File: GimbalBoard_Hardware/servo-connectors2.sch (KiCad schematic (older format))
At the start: 44 parts, among them Q1 Q_NMOS_GDS, Q2 Q_NMOS_GDS, Q3 Q_NMOS_GDS, Q4 Q_NMOS_GDS, Q5 Q_NMOS_GDS, Q6 Q_NMOS_GDS, Q7 Q_NMOS_GDS, Q8 Q_NMOS_GDS

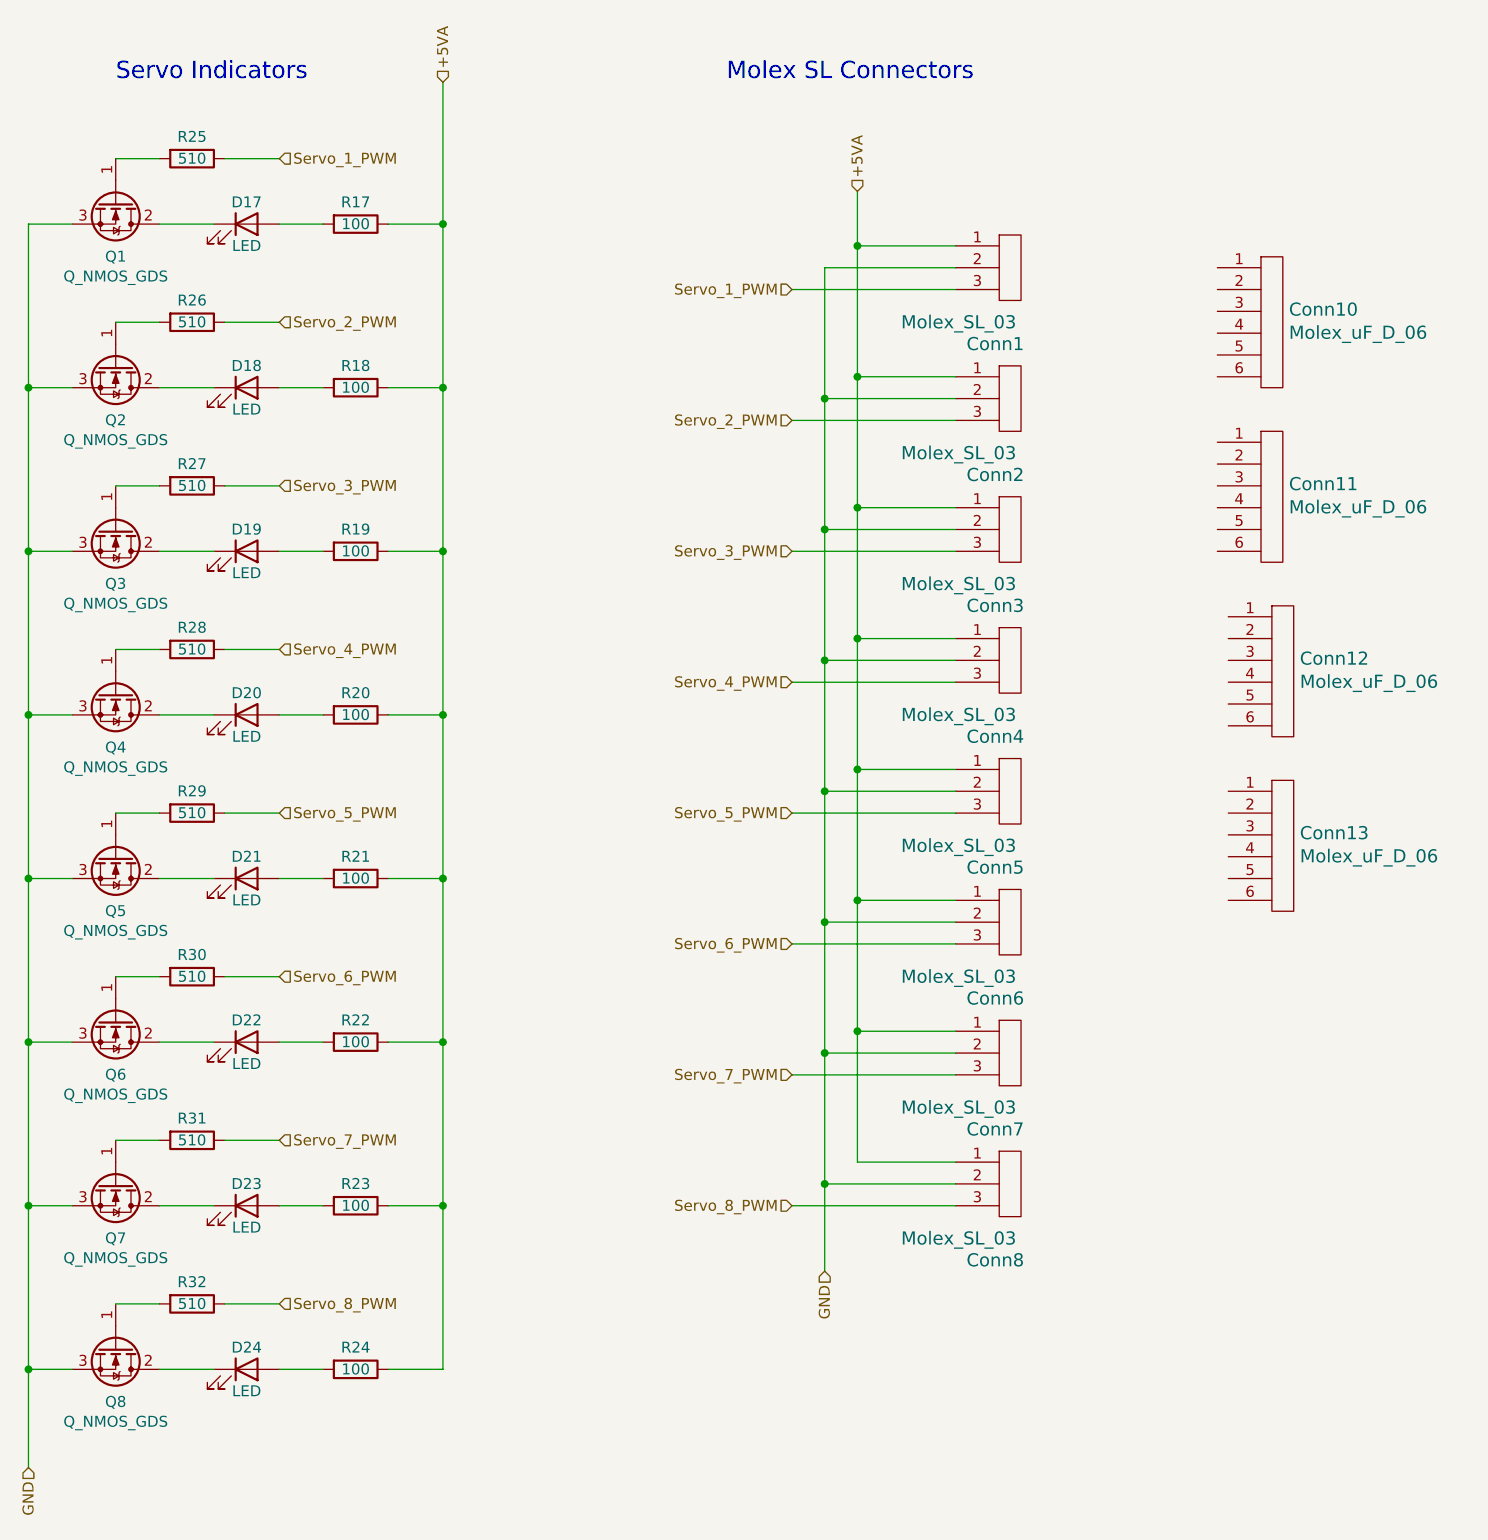
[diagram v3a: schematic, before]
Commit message: new connectors and decals
i have the 3x2 molex on here as well as some cowboy bebop decals.
the swtich still needs be confirmed.
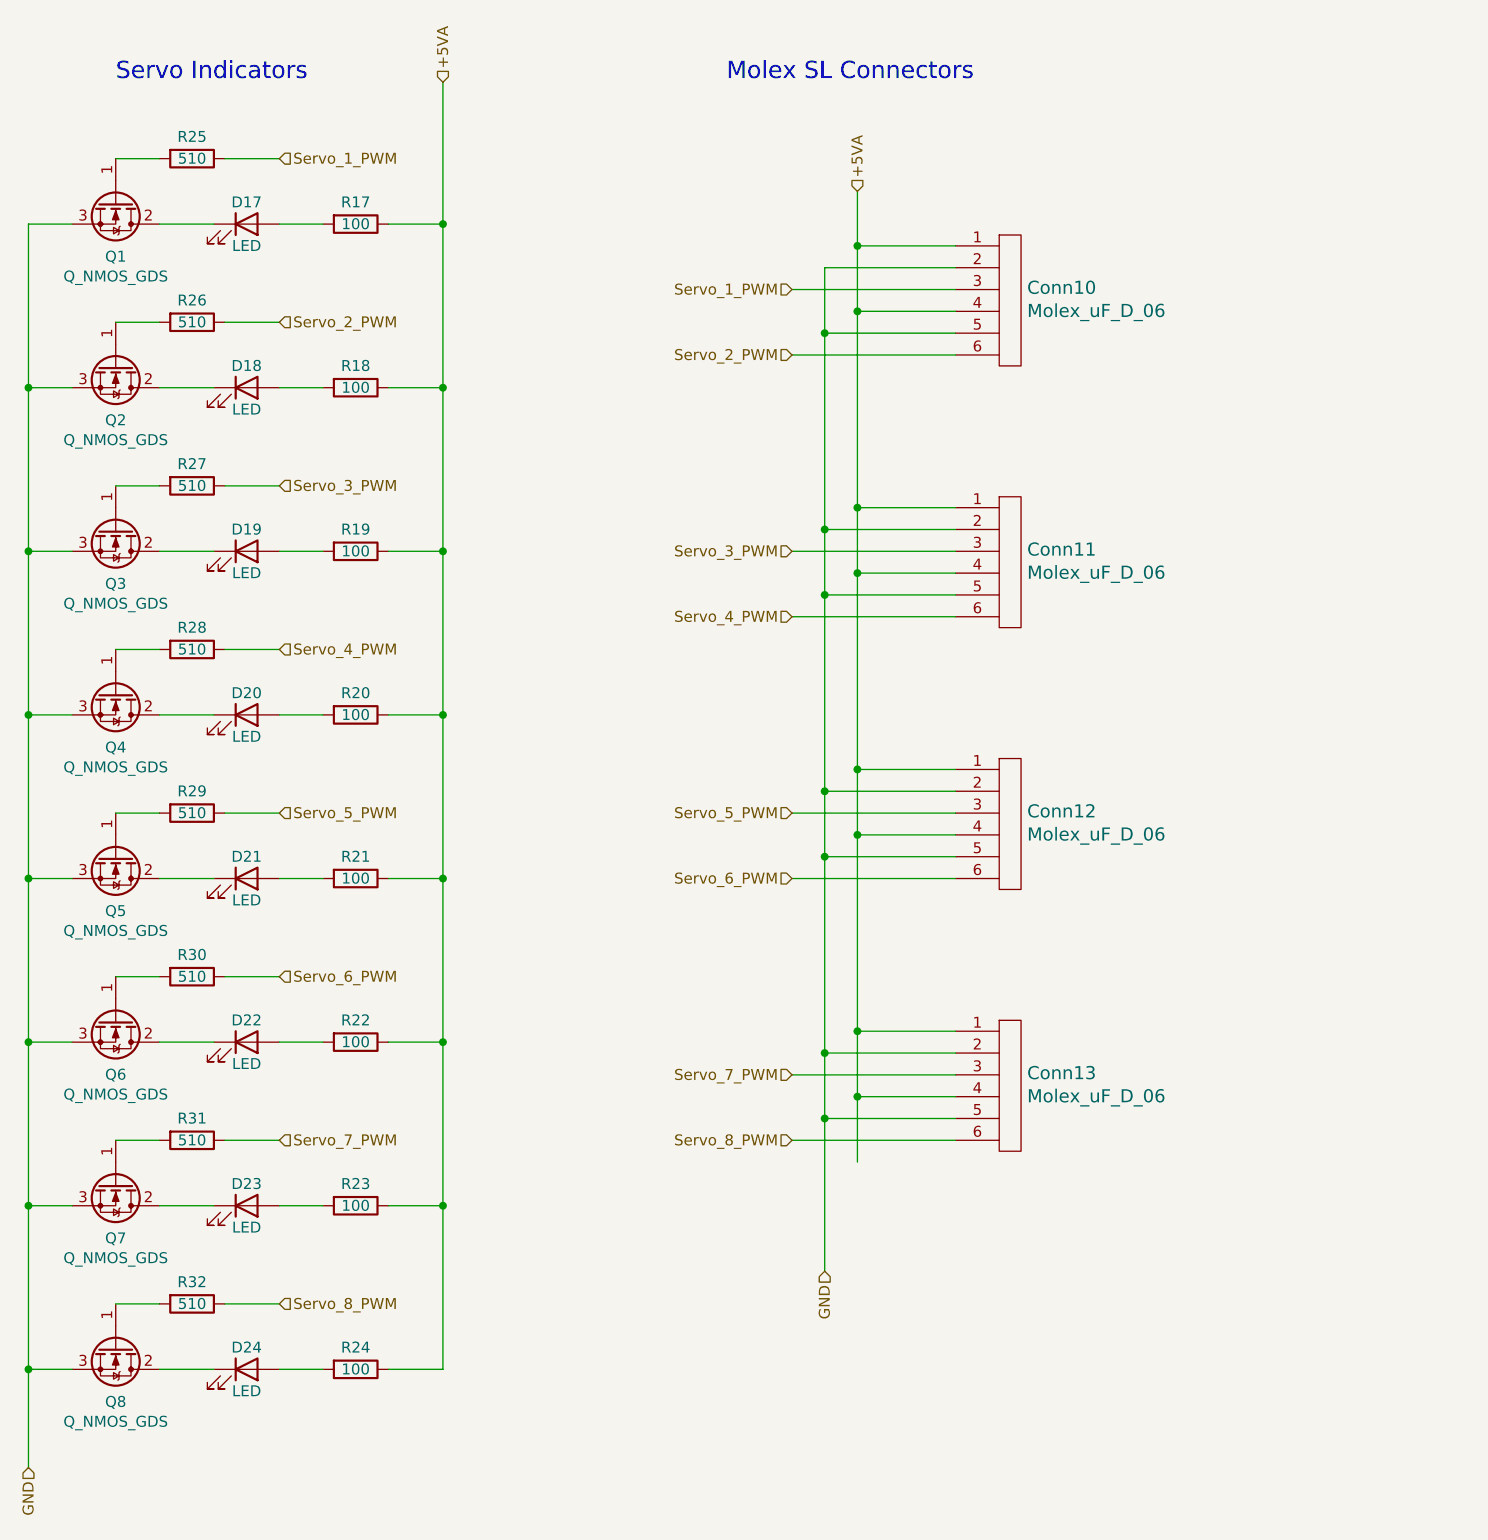
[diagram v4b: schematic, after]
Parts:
- removed Conn1, Conn2, Conn3, Conn4, Conn5, Conn6, Conn7, Conn8: Molex_SL_03, MRDT_Connectors:MOLEX_SL_03_Horizontal, symbol MRDT_Connectors:Molex_SL_03
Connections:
- net +5VA: now also Conn10.1, Conn10.4, Conn11.1, Conn11.4, Conn12.1, Conn12.4, Conn13.1, Conn13.4
- net GND: now also Conn10.2, Conn10.5, Conn11.2, Conn11.5, Conn12.2, Conn12.5, Conn13.2, Conn13.5
- net Servo_1_PWM: now also Conn10.3
- net Servo_2_PWM: now also Conn10.6
- net Servo_3_PWM: now also Conn11.3
- net Servo_4_PWM: now also Conn11.6
- net Servo_5_PWM: now also Conn12.3
- net Servo_6_PWM: now also Conn12.6
- net Servo_7_PWM: now also Conn13.3
- net Servo_8_PWM: now also Conn13.6
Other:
- moved on the sheet: Conn10, Conn11, Conn12, Conn13
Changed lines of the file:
@@
 Text HLabel 5000 6450 3    50   Input ~ 0
 GND
-Text HLabel 4850 6150 0    50   Input ~ 0
+Text HLabel 4850 5850 0    50   Input ~ 0
 Servo_8_PWM
-Connection ~ 5000 6050
 Wire Wire Line
-	5000 6050 5000 6450
+	5600 5850 4850 5850
 Wire Wire Line
-	5600 6150 4850 6150
+	5600 5750 5000 5750
 Wire Wire Line
-	5600 6050 5000 6050
-Wire Wire Line
-	5600 5950 5150 5950
-$Comp
-L MRDT_Connectors:Molex_SL_03 Conn?
-U 1 1 617A1B6D
-P 5800 6200
-AR Path="/615E206C/617A1B6D" Ref="Conn?"  Part="1"
-AR Path="/6178B814/617A1B6D" Ref="Conn8"  Part="1"
-F 0 "Conn8" H 5650 6000 60  0000 L CNN
-F 1 "Molex_SL_03" H 5350 6100 60  0000 L CNN
-F 2 "MRDT_Connectors:MOLEX_SL_03_Horizontal" H 5800 6200 60  0001 C CNN
-F 3 "" H 5800 6200 60  0001 C CNN
-	1    5800 6200
-	1    0    0    -1
-$EndComp
-$Comp
-L MRDT_Connectors:Molex_SL_03 Conn?
-U 1 1 617A1B73
-P 5800 5600
-AR Path="/615E206C/617A1B73" Ref="Conn?"  Part="1"
-AR Path="/6178B814/617A1B73" Ref="Conn7"  Part="1"
-F 0 "Conn7" H 5650 5400 60  0000 L CNN
-F 1 "Molex_SL_03" H 5350 5500 60  0000 L CNN
-F 2 "MRDT_Connectors:MOLEX_SL_03_Horizontal" H 5800 5600 60  0001 C CNN
-F 3 "" H 5800 5600 60  0001 C CNN
-	1    5800 5600
-	1    0    0    -1
-$EndComp
+	5600 5650 5150 5650
 Text HLabel 4850 5550 0    50   Input ~ 0
 Servo_7_PWM
 Connection ~ 5000 5450
 Wire Wire Line
-	5000 6050 5000 5450
-Wire Wire Line
-	5150 5350 5150 5950
+	5150 5350 5150 5650
 Connection ~ 5150 5350
 Wire Wire Line
@@
 Wire Wire Line
 	5600 5350 5150 5350
-Text HLabel 4850 4950 0    50   Input ~ 0
+Text HLabel 4850 4650 0    50   Input ~ 0
 Servo_6_PWM
-Connection ~ 5000 4850
 Wire Wire Line
-	5000 5450 5000 4850
+	5600 4650 4850 4650
 Wire Wire Line
-	5150 4750 5150 5350
-Connection ~ 5150 4750
+	5600 4550 5000 4550
 Wire Wire Line
-	5600 4950 4850 4950
-Wire Wire Line
-	5600 4850 5000 4850
-Wire Wire Line
-	5600 4750 5150 4750
-$Comp
-L MRDT_Connectors:Molex_SL_03 Conn?
-U 1 1 617A1B79
-P 5800 5000
-AR Path="/615E206C/617A1B79" Ref="Conn?"  Part="1"
-AR Path="/6178B814/617A1B79" Ref="Conn6"  Part="1"
-F 0 "Conn6" H 5650 4800 60  0000 L CNN
-F 1 "Molex_SL_03" H 5350 4900 60  0000 L CNN
-F 2 "MRDT_Connectors:MOLEX_SL_03_Horizontal" H 5800 5000 60  0001 C CNN
-F 3 "" H 5800 5000 60  0001 C CNN
-	1    5800 5000
-	1    0    0    -1
-$EndComp
+	5600 4450 5150 4450
 Text HLabel 4850 4350 0    50   Input ~ 0
 Servo_5_PWM
-Connection ~ 5000 4250
 Wire Wire Line
-	5000 4850 5000 4250
-Wire Wire Line
-	5150 4150 5150 4750
-Connection ~ 5150 4150
+	5150 4150 5150 4450
 Wire Wire Line
 	5600 4350 4850 4350
@@
 Wire Wire Line
 	5600 4150 5150 4150
-$Comp
-L MRDT_Connectors:Molex_SL_03 Conn?
-U 1 1 617A1B7F
-P 5800 4400
-AR Path="/615E206C/617A1B7F" Ref="Conn?"  Part="1"
-AR Path="/6178B814/617A1B7F" Ref="Conn5"  Part="1"
-F 0 "Conn5" H 5650 4200 60  0000 L CNN
-F 1 "Molex_SL_03" H 5350 4300 60  0000 L CNN
-F 2 "MRDT_Connectors:MOLEX_SL_03_Horizontal" H 5800 4400 60  0001 C CNN
-F 3 "" H 5800 4400 60  0001 C CNN
-	1    5800 4400
-	1    0    0    -1
-$EndComp
-Text HLabel 4850 3750 0    50   Input ~ 0
-Servo_4_PWM
-Connection ~ 5000 3650
-Wire Wire Line
-	5000 4250 5000 3650
-Wire Wire Line
-	5150 3550 5150 4150
-Connection ~ 5150 3550
-Wire Wire Line
-	5600 3750 4850 3750
-Wire Wire Line
-	5600 3650 5000 3650
-Wire Wire Line
-	5600 3550 5150 3550
-$Comp
-L MRDT_Connectors:Molex_SL_03 Conn?
-U 1 1 617A1B85
-P 5800 3800
-AR Path="/615E206C/617A1B85" Ref="Conn?"  Part="1"
-AR Path="/6178B814/617A1B85" Ref="Conn4"  Part="1"
-F 0 "Conn4" H 5650 3600 60  0000 L CNN
-F 1 "Molex_SL_03" H 5350 3700 60  0000 L CNN
-F 2 "MRDT_Connectors:MOLEX_SL_03_Horizontal" H 5800 3800 60  0001 C CNN
-F 3 "" H 5800 3800 60  0001 C CNN
-	1    5800 3800
-	1    0    0    -1
-$EndComp
 Text HLabel 4850 3150 0    50   Input ~ 0
 Servo_3_PWM
-Connection ~ 5150 2950
+Text HLabel 4850 2250 0    50   Input ~ 0
+Servo_2_PWM
 Wire Wire Line
-	5150 2950 5150 3550
+	5150 1750 5150 2050
 Wire Wire Line
-	5000 3650 5000 3050
-Connection ~ 5000 3050
+	5600 2250 4850 2250
 Wire Wire Line
-	5600 2950 5150 2950
+	5600 2150 5000 2150
 Wire Wire Line
-	5600 3050 5000 3050
-Wire Wire Line
-	5600 3150 4850 3150
+	5600 2050 5150 2050
 $Comp
-L MRDT_Connectors:Molex_SL_03 Conn?
-U 1 1 617A1B8B
-P 5800 3200
-AR Path="/615E206C/617A1B8B" Ref="Conn?"  Part="1"
-AR Path="/6178B814/617A1B8B" Ref="Conn3"  Part="1"
-F 0 "Conn3" H 5650 3000 60  0000 L CNN
-F 1 "Molex_SL_03" H 5350 3100 60  0000 L CNN
-F 2 "MRDT_Connectors:MOLEX_SL_03_Horizontal" H 5800 3200 60  0001 C CNN
-F 3 "" H 5800 3200 60  0001 C CNN
-	1    5800 3200
-	1    0    0    -1
-$EndComp
-Text HLabel 4850 2550 0    50   Input ~ 0
-Servo_2_PWM
-Connection ~ 5000 2450
-Wire Wire Line
-	5000 3050 5000 2450
-Wire Wire Line
-	5150 2350 5150 2950
-Connection ~ 5150 2350
-Wire Wire Line
-	5150 1750 5150 2350
-Wire Wire Line
-	5000 2450 5000 1850
-Wire Wire Line
-	5600 2550 4850 2550
-Wire Wire Line
-	5600 2450 5000 2450
-Wire Wire Line
-	5600 2350 5150 2350
-$Comp
-L MRDT_Connectors:Molex_SL_03 Conn?
-U 1 1 617A1B91
-P 5800 2600
-AR Path="/615E206C/617A1B91" Ref="Conn?"  Part="1"
-AR Path="/6178B814/617A1B91" Ref="Conn2"  Part="1"
-F 0 "Conn2" H 5650 2400 60  0000 L CNN
-F 1 "Molex_SL_03" H 5350 2500 60  0000 L CNN
-F 2 "MRDT_Connectors:MOLEX_SL_03_Horizontal" H 5800 2600 60  0001 C CNN
-F 3 "" H 5800 2600 60  0001 C CNN
-	1    5800 2600
+L MRDT_Connectors:Molex_uF_D_06 Conn13
+U 1 1 61A5F2E6
+P 5800 6100
+F 0 "Conn13" H 5928 6658 60  0000 L CNN
+F 1 "Molex_uF_D_06" H 5928 6552 60  0000 L CNN
+F 2 "MRDT_Connectors:MOLEX_uF_D_06_Horizontal" H 5800 6400 60  0001 C CNN
+F 3 "" H 5800 6400 60  0001 C CNN
+	1    5800 6100
 	1    0    0    -1
 $EndComp
 $Comp
-L MRDT_Connectors:Molex_SL_03 Conn?
-U 1 1 617A1B97
-P 5800 2000
-AR Path="/615E206C/617A1B97" Ref="Conn?"  Part="1"
-AR Path="/6178B814/617A1B97" Ref="Conn1"  Part="1"
-F 0 "Conn1" H 5650 1800 60  0000 L CNN
-F 1 "Molex_SL_03" H 5350 1900 60  0000 L CNN
-F 2 "MRDT_Connectors:MOLEX_SL_03_Horizontal" H 5800 2000 60  0001 C CNN
-F 3 "" H 5800 2000 60  0001 C CNN
-	1    5800 2000
+L MRDT_Connectors:Molex_uF_D_06 Conn12
+U 1 1 61A5BF21
+P 5800 4900
+F 0 "Conn12" H 5928 5458 60  0000 L CNN
+F 1 "Molex_uF_D_06" H 5928 5352 60  0000 L CNN
+F 2 "MRDT_Connectors:MOLEX_uF_D_06_Horizontal" H 5800 5200 60  0001 C CNN
+F 3 "" H 5800 5200 60  0001 C CNN
+	1    5800 4900
 	1    0    0    -1
 $EndComp
@@
 L MRDT_Connectors:Molex_uF_D_06 Conn10
 U 1 1 61A57BF2
-P 7000 2600
-F 0 "Conn10" H 7128 3158 60  0000 L CNN
-F 1 "Molex_uF_D_06" H 7128 3052 60  0000 L CNN
-F 2 "MRDT_Connectors:MOLEX_uF_D_06_Horizontal" H 7000 2900 60  0001 C CNN
-F 3 "" H 7000 2900 60  0001 C CNN
-	1    7000 2600
+P 5800 2500
+F 0 "Conn10" H 5928 3058 60  0000 L CNN
+F 1 "Molex_uF_D_06" H 5928 2952 60  0000 L CNN
+F 2 "MRDT_Connectors:MOLEX_uF_D_06_Horizontal" H 5800 2800 60  0001 C CNN
+F 3 "" H 5800 2800 60  0001 C CNN
+	1    5800 2500
 	1    0    0    -1
 $EndComp
+Connection ~ 5000 2150
+Wire Wire Line
+	5000 2150 5000 1850
+Connection ~ 5150 2050
+Wire Wire Line
+	5000 2150 5000 3050
+Wire Wire Line
+	5150 2050 5150 2950
+Connection ~ 5000 3050
+Connection ~ 5150 2950
+Connection ~ 5150 4150
+Connection ~ 5000 4250
+Wire Wire Line
+	5600 3150 4850 3150
+Wire Wire Line
+	5600 3050 5000 3050
+Wire Wire Line
+	5600 2950 5150 2950
 $Comp
 L MRDT_Connectors:Molex_uF_D_06 Conn11
 U 1 1 61A58E08
-P 7000 3400
-F 0 "Conn11" H 7128 3958 60  0000 L CNN
-F 1 "Molex_uF_D_06" H 7128 3852 60  0000 L CNN
-F 2 "MRDT_Connectors:MOLEX_uF_D_06_Horizontal" H 7000 3700 60  0001 C CNN
-F 3 "" H 7000 3700 60  0001 C CNN
-	1    7000 3400
+P 5800 3700
+F 0 "Conn11" H 5928 4258 60  0000 L CNN
+F 1 "Molex_uF_D_06" H 5928 4152 60  0000 L CNN
+F 2 "MRDT_Connectors:MOLEX_uF_D_06_Horizontal" H 5800 4000 60  0001 C CNN
+F 3 "" H 5800 4000 60  0001 C CNN
+	1    5800 3700
 	1    0    0    -1
 $EndComp
-$Comp
-L MRDT_Connectors:Molex_uF_D_06 Conn12
-U 1 1 61A5BF21
-P 7050 4200
-F 0 "Conn12" H 7178 4758 60  0000 L CNN
-F 1 "Molex_uF_D_06" H 7178 4652 60  0000 L CNN
-F 2 "MRDT_Connectors:MOLEX_uF_D_06_Horizontal" H 7050 4500 60  0001 C CNN
-F 3 "" H 7050 4500 60  0001 C CNN
-	1    7050 4200
-	1    0    0    -1
-$EndComp
-$Comp
-L MRDT_Connectors:Molex_uF_D_06 Conn13
-U 1 1 61A5F2E6
-P 7050 5000
-F 0 "Conn13" H 7178 5558 60  0000 L CNN
-F 1 "Molex_uF_D_06" H 7178 5452 60  0000 L CNN
-F 2 "MRDT_Connectors:MOLEX_uF_D_06_Horizontal" H 7050 5300 60  0001 C CNN
-F 3 "" H 7050 5300 60  0001 C CNN
-	1    7050 5000
-	1    0    0    -1
-$EndComp
+Wire Wire Line
+	5150 2950 5150 3250
+Wire Wire Line
+	5600 3250 5150 3250
+Wire Wire Line
+	5600 3350 5000 3350
+Wire Wire Line
+	5600 3450 4850 3450
+Text HLabel 4850 3450 0    50   Input ~ 0
+Servo_4_PWM
+Connection ~ 5000 3350
+Wire Wire Line
+	5000 3350 5000 3050
+Connection ~ 5150 3250
+Wire Wire Line
+	5000 3350 5000 4250
+Wire Wire Line
+	5150 3250 5150 4150
+Connection ~ 5000 4550
+Wire Wire Line
+	5000 4550 5000 4250
+Connection ~ 5150 4450
+Wire Wire Line
+	5000 4550 5000 5450
+Wire Wire Line
+	5150 4450 5150 5350
+Connection ~ 5000 5750
+Wire Wire Line
+	5000 5750 5000 5450
+Connection ~ 5150 5650
+Wire Wire Line
+	5150 5650 5150 5950
+Wire Wire Line
+	5000 5750 5000 6450
 $EndSCHEMATC
